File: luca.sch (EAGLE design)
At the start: 56 parts

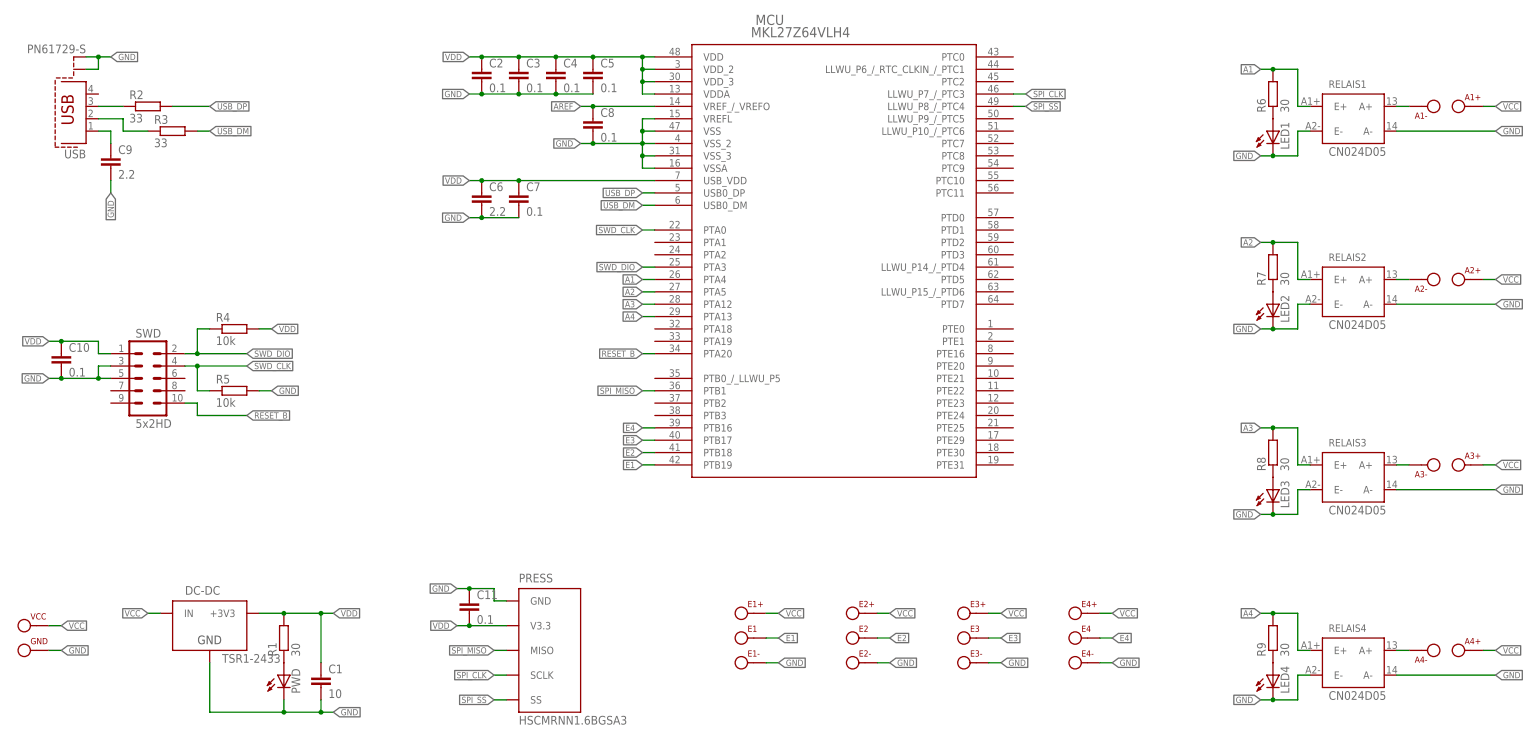
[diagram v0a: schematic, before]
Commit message: ESD, added Pull-Rs, refactored Dimensions
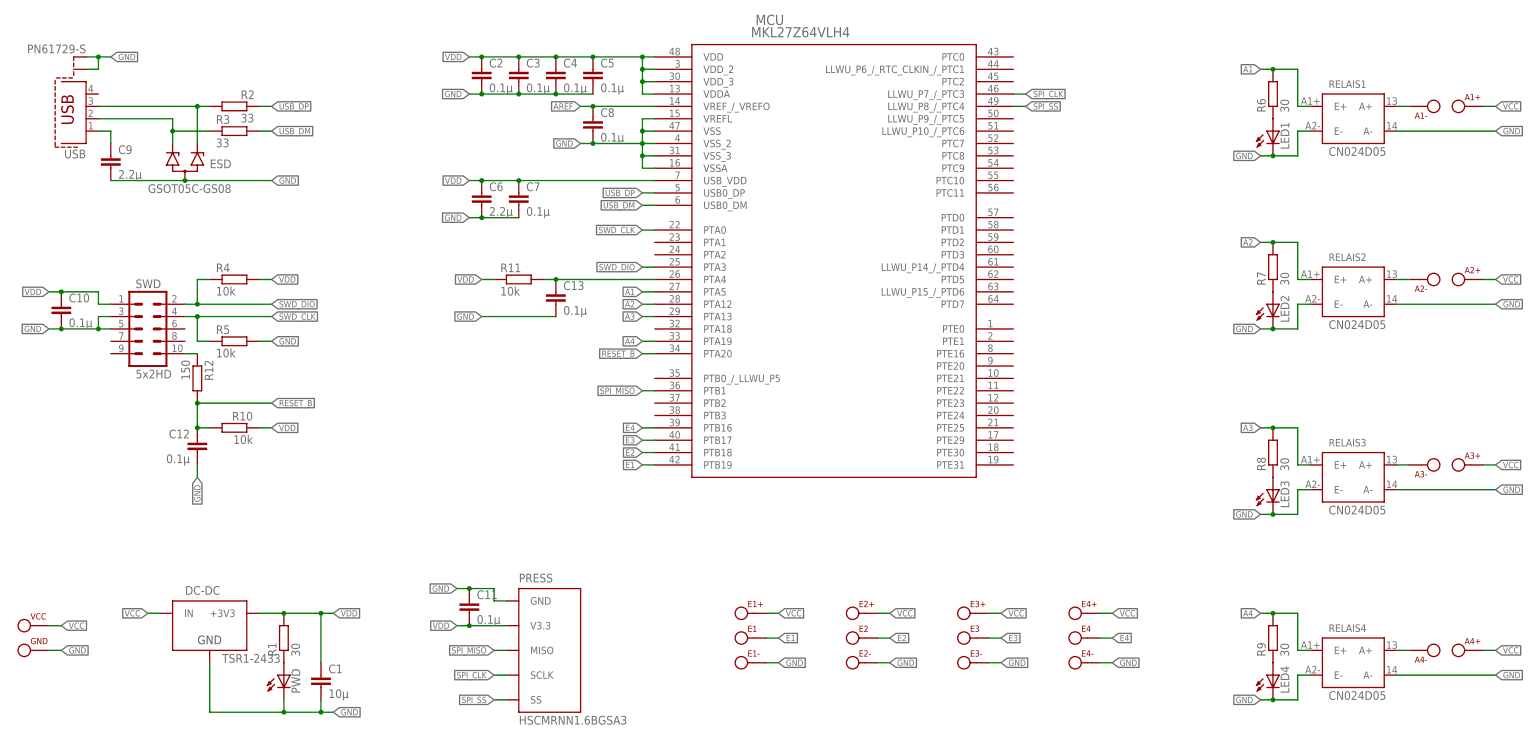
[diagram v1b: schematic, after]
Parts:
- added C12, C13: 0.1µ, rcl:C-EUC1206
- added ESD: GSOT05C-GS08, GSOT05C-GS08:GSOT05C-GS08
- added R10, R11: 10k, rcl:R-EU_M1206
- added R12: 150, rcl:R-EU_M1206
- C1: value 10 -> 10µ
- C10, C11, C2, C3, C4, C5, C7, C8: value 0.1 -> 0.1µ
- C6, C9: value 2.2 -> 2.2µ
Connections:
- new net N$15: R12.1, SWD.10
- new net NMI_B: C13.1, MCU.PTA4, R11.2
- net A1: now also MCU.PTA5; no longer MCU.PTA4
- net A2: now also MCU.PTA12; no longer MCU.PTA5
- net A3: now also MCU.PTA13; no longer MCU.PTA12
- net A4: now also MCU.PTA19; no longer MCU.PTA13
- net GND: now also C12.2, C13.2, ESD.P$3
- net N$1: now also ESD.P$2
- net N$2: now also ESD.P$1
- net RESET_B: now also C12.1, R10.2, R12.2; no longer SWD.10
- net VDD: now also R10.1, R11.1
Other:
- moved on the sheet: C10, R2, R3, R4, R5, SWD

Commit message: removed unnecessary caps, green LEDs R -> 100
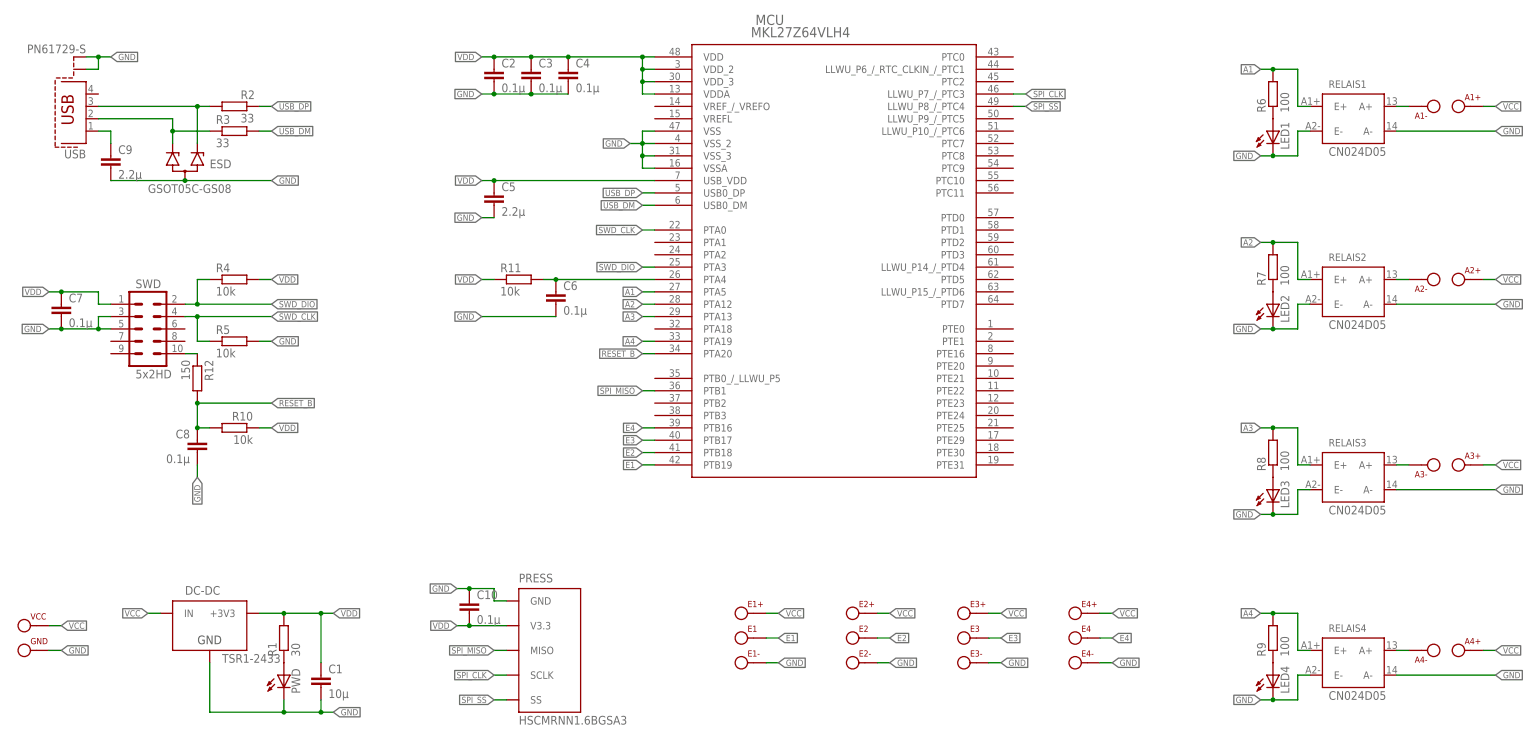
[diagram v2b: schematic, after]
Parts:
- removed C11, C12, C13: 0.1µ, rcl:C-EUC1206
- C5: value 0.1µ -> 2.2µ
- C6: value 2.2µ -> 0.1µ
- R6, R7, R8, R9: value 30 -> 100
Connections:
- removed net AREF: C8.1, MCU.VREF_/_VREFO
- net GND: now also C10.1; no longer C10.2, C11.1, C12.2, C13.2, MCU.VREFL
- net NMI_B: now also C6.1; no longer C13.1
- net RESET_B: now also C8.1; no longer C12.1
- net VDD: now also C10.2; no longer C10.1, C11.2, C6.1
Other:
- moved on the sheet: C10, C2, C3, C4, C5, C6, C7, C8

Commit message: added config jumper
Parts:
- added J1: (no value), SparkFun-Connectors:M02LOCK
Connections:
- new net N$12: J1.1, MCU.PTE24
- new net N$13: J1.2, MCU.PTE25
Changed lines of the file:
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@@
 <part name="C6" library="rcl" deviceset="C-EU" device="C1206" value="0.1µ"/>
 <part name="ESD" library="GSOT05C-GS08" deviceset="GSOT05C-GS08" device=""/>
+<part name="J1" library="SparkFun-Connectors" deviceset="M02" device="LOCK"/>
 </parts>
 <sheets>
@@
 <attribute name="NAME" x="-55.88" y="81.28" size="1.778" layer="95"/>
 </instance>
+<instance part="J1" gate="G$1" x="119.38" y="30.48" rot="R180"/>
 </instances>
 <busses>
@@
 </segment>
 </net>
+<net name="N$12" class="0">
+<segment>
+<pinref part="MCU" gate="A" pin="PTE24"/>
+<pinref part="J1" gate="G$1" pin="1"/>
+<wire x1="111.76" y1="30.48" x2="109.22" y2="30.48" width="0.1524" layer="91"/>
+</segment>
+</net>
+<net name="N$13" class="0">
+<segment>
+<pinref part="MCU" gate="A" pin="PTE25"/>
+<pinref part="J1" gate="G$1" pin="2"/>
+<wire x1="111.76" y1="27.94" x2="109.22" y2="27.94" width="0.1524" layer="91"/>
+</segment>
+</net>

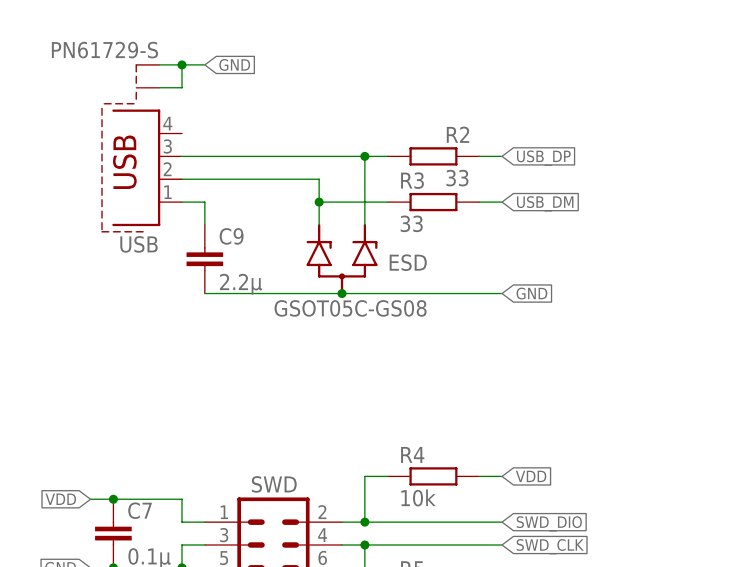
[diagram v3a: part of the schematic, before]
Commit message: Refactoring ESD, NMI
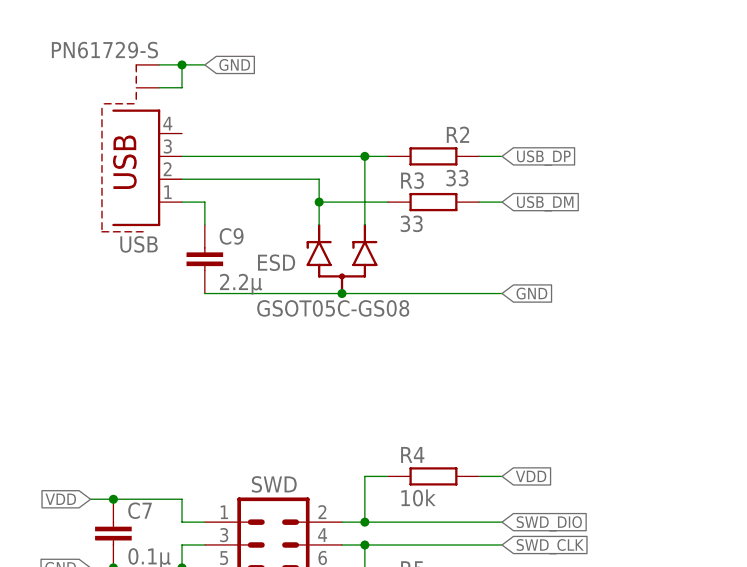
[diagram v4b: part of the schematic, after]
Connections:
- net N$1: now also ESD.P$1; no longer ESD.P$2
- net N$2: now also ESD.P$2; no longer ESD.P$1
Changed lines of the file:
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@@
 <instance part="R12" gate="G$1" x="-58.42" y="38.1" rot="R270"/>
 <instance part="C6" gate="G$1" x="15.24" y="55.88"/>
-<instance part="ESD" gate="G$1" x="-60.96" y="83.82" smashed="yes">
-<attribute name="VALUE" x="-68.58" y="76.2" size="1.778" layer="96"/>
-<attribute name="NAME" x="-55.88" y="81.28" size="1.778" layer="95"/>
+<instance part="ESD" gate="G$1" x="-60.96" y="83.82" smashed="yes" rot="MR0">
+<attribute name="VALUE" x="-53.34" y="76.2" size="1.778" layer="96" rot="MR0"/>
+<attribute name="NAME" x="-66.04" y="81.28" size="1.778" layer="95" rot="MR0"/>
 </instance>
 <instance part="J1" gate="G$1" x="119.38" y="30.48" rot="R180"/>
@@
 <pinref part="USB" gate="G$1" pin="3"/>
 <wire x1="-55.88" y1="93.98" x2="-58.42" y2="93.98" width="0.1524" layer="91"/>
-<pinref part="ESD" gate="G$1" pin="P$2"/>
+<pinref part="ESD" gate="G$1" pin="P$1"/>
 <wire x1="-58.42" y1="93.98" x2="-78.74" y2="93.98" width="0.1524" layer="91"/>
 <wire x1="-58.42" y1="86.36" x2="-58.42" y2="93.98" width="0.1524" layer="91"/>
@@
 <net name="N$2" class="0">
 <segment>
-<pinref part="ESD" gate="G$1" pin="P$1"/>
-<wire x1="-63.5" y1="86.36" x2="-63.5" y2="88.9" width="0.1524" layer="91"/>
 <pinref part="R3" gate="G$1" pin="1"/>
 <wire x1="-63.5" y1="88.9" x2="-55.88" y2="88.9" width="0.1524" layer="91"/>
@@
 <pinref part="USB" gate="G$1" pin="2"/>
 <wire x1="-63.5" y1="91.44" x2="-78.74" y2="91.44" width="0.1524" layer="91"/>
+<pinref part="ESD" gate="G$1" pin="P$2"/>
+<wire x1="-63.5" y1="86.36" x2="-63.5" y2="88.9" width="0.1524" layer="91"/>
 <junction x="-63.5" y="88.9"/>
 </segment>
